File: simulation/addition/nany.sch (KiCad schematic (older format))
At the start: 6 parts, among them M2 MPMOS, M3 MPMOS, M4 MNMOS, M5 MNMOS

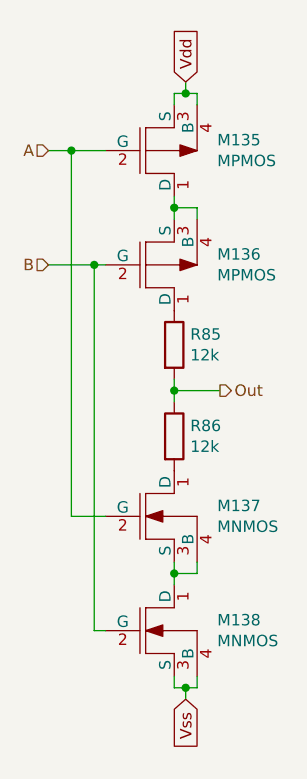
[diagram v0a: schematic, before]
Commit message: remove nconensus gate from sum gate, removed .sch-bak and cache files
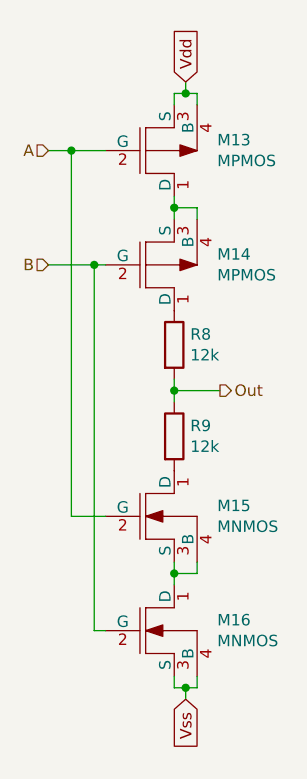
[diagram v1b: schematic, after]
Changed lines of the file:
@@
 $Descr A4 11693 8268
 encoding utf-8
-Sheet 7 28
+Sheet 7 26
 Title ""
 Date ""
@@
 AR Path="/5FDE2F92/5FDD79FE/5FEDF3F0/600EB164/5FFEAE4F" Ref="M606"  Part="1"
 AR Path="/5FDE2F92/5FDD8DDE/5FFEAE4F" Ref="M626"  Part="1"
-F 0 "M136" H 5688 3396 50  0000 L CNN
+AR Path="/5FDC5271/600A11DE/5FFEAE4F" Ref="M6"  Part="1"
+AR Path="/5FDC5271/600E751A/5FFEAE4F" Ref="M10"  Part="1"
+AR Path="/5FDC5271/600EB164/5FFEAE4F" Ref="M14"  Part="1"
+F 0 "M14" H 5688 3396 50  0000 L CNN
 F 1 "MPMOS" H 5688 3305 50  0000 L CNN
 F 2 "" H 5400 3350 50  0001 C CNN
@@
 AR Path="/5FDE2F92/5FDD79FE/5FEDF3F0/600EB164/5FFEAE59" Ref="M607"  Part="1"
 AR Path="/5FDE2F92/5FDD8DDE/5FFEAE59" Ref="M627"  Part="1"
-F 0 "M137" H 5688 4496 50  0000 L CNN
+AR Path="/5FDC5271/600A11DE/5FFEAE59" Ref="M7"  Part="1"
+AR Path="/5FDC5271/600E751A/5FFEAE59" Ref="M11"  Part="1"
+AR Path="/5FDC5271/600EB164/5FFEAE59" Ref="M15"  Part="1"
+F 0 "M15" H 5688 4496 50  0000 L CNN
 F 1 "MNMOS" H 5688 4405 50  0000 L CNN
 F 2 "" H 5375 4450 50  0001 C CNN
@@
 AR Path="/5FDE2F92/5FDD79FE/5FEDF3F0/600EB164/5FFEAE68" Ref="R380"  Part="1"
 AR Path="/5FDE2F92/5FDD8DDE/5FFEAE68" Ref="R394"  Part="1"
-F 0 "R86" H 5570 4146 50  0000 L CNN
+AR Path="/5FDC5271/600A11DE/5FFEAE68" Ref="R5"  Part="1"
+AR Path="/5FDC5271/600E751A/5FFEAE68" Ref="R7"  Part="1"
+AR Path="/5FDC5271/600EB164/5FFEAE68" Ref="R9"  Part="1"
+F 0 "R9" H 5570 4146 50  0000 L CNN
 F 1 "12k" H 5570 4055 50  0000 L CNN
 F 2 "" V 5430 4100 50  0001 C CNN
@@
 AR Path="/5FDE2F92/5FDD79FE/5FEDF3F0/600EB164/5FFEAE6E" Ref="R379"  Part="1"
 AR Path="/5FDE2F92/5FDD8DDE/5FFEAE6E" Ref="R393"  Part="1"
-F 0 "R85" H 5570 3746 50  0000 L CNN
+AR Path="/5FDC5271/600A11DE/5FFEAE6E" Ref="R4"  Part="1"
+AR Path="/5FDC5271/600E751A/5FFEAE6E" Ref="R6"  Part="1"
+AR Path="/5FDC5271/600EB164/5FFEAE6E" Ref="R8"  Part="1"
+F 0 "R8" H 5570 3746 50  0000 L CNN
 F 1 "12k" H 5570 3655 50  0000 L CNN
 F 2 "" V 5430 3700 50  0001 C CNN
@@
 AR Path="/5FDE2F92/5FDD79FE/5FEDF3F0/600EB164/5FFEAE7E" Ref="M608"  Part="1"
 AR Path="/5FDE2F92/5FDD8DDE/5FFEAE7E" Ref="M628"  Part="1"
-F 0 "M138" H 5688 4996 50  0000 L CNN
+AR Path="/5FDC5271/600A11DE/5FFEAE7E" Ref="M8"  Part="1"
+AR Path="/5FDC5271/600E751A/5FFEAE7E" Ref="M12"  Part="1"
+AR Path="/5FDC5271/600EB164/5FFEAE7E" Ref="M16"  Part="1"
+F 0 "M16" H 5688 4996 50  0000 L CNN
 F 1 "MNMOS" H 5688 4905 50  0000 L CNN
 F 2 "" H 5375 4950 50  0001 C CNN
@@
 AR Path="/5FDE2F92/5FDD79FE/5FEDF3F0/600EB164/5FFEAE96" Ref="M605"  Part="1"
 AR Path="/5FDE2F92/5FDD8DDE/5FFEAE96" Ref="M625"  Part="1"
-F 0 "M135" H 5688 2896 50  0000 L CNN
+AR Path="/5FDC5271/600A11DE/5FFEAE96" Ref="M5"  Part="1"
+AR Path="/5FDC5271/600E751A/5FFEAE96" Ref="M9"  Part="1"
+AR Path="/5FDC5271/600EB164/5FFEAE96" Ref="M13"  Part="1"
+F 0 "M13" H 5688 2896 50  0000 L CNN
 F 1 "MPMOS" H 5688 2805 50  0000 L CNN
 F 2 "" H 5400 2850 50  0001 C CNN

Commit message: lowered transistor count for sum gate
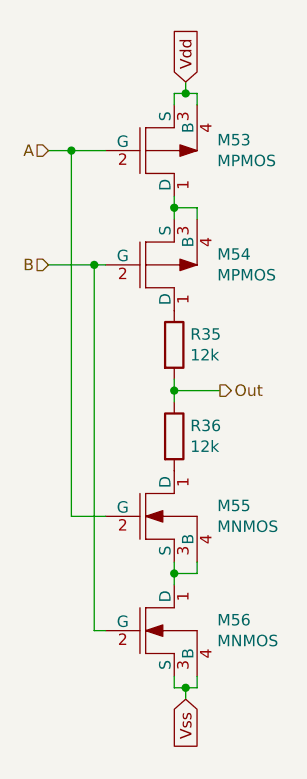
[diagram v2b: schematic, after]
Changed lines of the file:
@@
 $Descr A4 11693 8268
 encoding utf-8
-Sheet 7 26
+Sheet 7 24
 Title ""
 Date ""
@@
 AR Path="/5FDC5271/600E751A/5FFEAE4F" Ref="M10"  Part="1"
 AR Path="/5FDC5271/600EB164/5FFEAE4F" Ref="M14"  Part="1"
-F 0 "M14" H 5688 3396 50  0000 L CNN
+AR Path="/5FDCD92F/600A11DE/5FFEAE4F" Ref="M6"  Part="1"
+AR Path="/5FDCD92F/600E751A/5FFEAE4F" Ref="M10"  Part="1"
+AR Path="/5FDCD92F/600EB164/5FFEAE4F" Ref="M14"  Part="1"
+AR Path="/5FDCD92F/5FDCFF59/5FFEAE4F" Ref="M?"  Part="1"
+AR Path="/5FDD3C70/5FDA8800/5FEDF3F0/600A11DE/5FFEAE4F" Ref="M2"  Part="1"
+AR Path="/5FDD3C70/5FDA8800/5FEDF3F0/600E751A/5FFEAE4F" Ref="M6"  Part="1"
+AR Path="/5FDD3C70/5FDA8800/5FEDF3F0/600EB164/5FFEAE4F" Ref="M10"  Part="1"
+AR Path="/5FDD3C70/5FDD79FE/5FEDF3F0/600A11DE/5FFEAE4F" Ref="M28"  Part="1"
+AR Path="/5FDD3C70/5FDD79FE/5FEDF3F0/600E751A/5FFEAE4F" Ref="M32"  Part="1"
+AR Path="/5FDD3C70/5FDD79FE/5FEDF3F0/600EB164/5FFEAE4F" Ref="M36"  Part="1"
+AR Path="/5FDD3C70/5FDD8DDE/5FFEAE4F" Ref="M54"  Part="1"
+F 0 "M54" H 5688 3396 50  0000 L CNN
 F 1 "MPMOS" H 5688 3305 50  0000 L CNN
 F 2 "" H 5400 3350 50  0001 C CNN
@@
 AR Path="/5FDC5271/600E751A/5FFEAE59" Ref="M11"  Part="1"
 AR Path="/5FDC5271/600EB164/5FFEAE59" Ref="M15"  Part="1"
-F 0 "M15" H 5688 4496 50  0000 L CNN
+AR Path="/5FDCD92F/600A11DE/5FFEAE59" Ref="M7"  Part="1"
+AR Path="/5FDCD92F/600E751A/5FFEAE59" Ref="M11"  Part="1"
+AR Path="/5FDCD92F/600EB164/5FFEAE59" Ref="M15"  Part="1"
+AR Path="/5FDCD92F/5FDCFF59/5FFEAE59" Ref="M?"  Part="1"
+AR Path="/5FDD3C70/5FDA8800/5FEDF3F0/600A11DE/5FFEAE59" Ref="M3"  Part="1"
+AR Path="/5FDD3C70/5FDA8800/5FEDF3F0/600E751A/5FFEAE59" Ref="M7"  Part="1"
+AR Path="/5FDD3C70/5FDA8800/5FEDF3F0/600EB164/5FFEAE59" Ref="M11"  Part="1"
+AR Path="/5FDD3C70/5FDD79FE/5FEDF3F0/600A11DE/5FFEAE59" Ref="M29"  Part="1"
+AR Path="/5FDD3C70/5FDD79FE/5FEDF3F0/600E751A/5FFEAE59" Ref="M33"  Part="1"
+AR Path="/5FDD3C70/5FDD79FE/5FEDF3F0/600EB164/5FFEAE59" Ref="M37"  Part="1"
+AR Path="/5FDD3C70/5FDD8DDE/5FFEAE59" Ref="M55"  Part="1"
+F 0 "M55" H 5688 4496 50  0000 L CNN
 F 1 "MNMOS" H 5688 4405 50  0000 L CNN
 F 2 "" H 5375 4450 50  0001 C CNN
@@
 AR Path="/5FDC5271/600E751A/5FFEAE68" Ref="R7"  Part="1"
 AR Path="/5FDC5271/600EB164/5FFEAE68" Ref="R9"  Part="1"
-F 0 "R9" H 5570 4146 50  0000 L CNN
+AR Path="/5FDCD92F/600A11DE/5FFEAE68" Ref="R6"  Part="1"
+AR Path="/5FDCD92F/600E751A/5FFEAE68" Ref="R8"  Part="1"
+AR Path="/5FDCD92F/600EB164/5FFEAE68" Ref="R10"  Part="1"
+AR Path="/5FDCD92F/5FDCFF59/5FFEAE68" Ref="R?"  Part="1"
+AR Path="/5FDD3C70/5FDA8800/5FEDF3F0/600A11DE/5FFEAE68" Ref="R3"  Part="1"
+AR Path="/5FDD3C70/5FDA8800/5FEDF3F0/600E751A/5FFEAE68" Ref="R6"  Part="1"
+AR Path="/5FDD3C70/5FDA8800/5FEDF3F0/600EB164/5FFEAE68" Ref="R8"  Part="1"
+AR Path="/5FDD3C70/5FDD79FE/5FEDF3F0/600A11DE/5FFEAE68" Ref="R20"  Part="1"
+AR Path="/5FDD3C70/5FDD79FE/5FEDF3F0/600E751A/5FFEAE68" Ref="R22"  Part="1"
+AR Path="/5FDD3C70/5FDD79FE/5FEDF3F0/600EB164/5FFEAE68" Ref="R24"  Part="1"
+AR Path="/5FDD3C70/5FDD8DDE/5FFEAE68" Ref="R36"  Part="1"
+F 0 "R36" H 5570 4146 50  0000 L CNN
 F 1 "12k" H 5570 4055 50  0000 L CNN
 F 2 "" V 5430 4100 50  0001 C CNN
@@
 AR Path="/5FDC5271/600E751A/5FFEAE6E" Ref="R6"  Part="1"
 AR Path="/5FDC5271/600EB164/5FFEAE6E" Ref="R8"  Part="1"
-F 0 "R8" H 5570 3746 50  0000 L CNN
+AR Path="/5FDCD92F/600A11DE/5FFEAE6E" Ref="R4"  Part="1"
+AR Path="/5FDCD92F/600E751A/5FFEAE6E" Ref="R7"  Part="1"
+AR Path="/5FDCD92F/600EB164/5FFEAE6E" Ref="R9"  Part="1"
+AR Path="/5FDCD92F/5FDCFF59/5FFEAE6E" Ref="R?"  Part="1"
+AR Path="/5FDD3C70/5FDA8800/5FEDF3F0/600A11DE/5FFEAE6E" Ref="R1"  Part="1"
+AR Path="/5FDD3C70/5FDA8800/5FEDF3F0/600E751A/5FFEAE6E" Ref="R4"  Part="1"
+AR Path="/5FDD3C70/5FDA8800/5FEDF3F0/600EB164/5FFEAE6E" Ref="R7"  Part="1"
+AR Path="/5FDD3C70/5FDD79FE/5FEDF3F0/600A11DE/5FFEAE6E" Ref="R19"  Part="1"
+AR Path="/5FDD3C70/5FDD79FE/5FEDF3F0/600E751A/5FFEAE6E" Ref="R21"  Part="1"
+AR Path="/5FDD3C70/5FDD79FE/5FEDF3F0/600EB164/5FFEAE6E" Ref="R23"  Part="1"
+AR Path="/5FDD3C70/5FDD8DDE/5FFEAE6E" Ref="R35"  Part="1"
+F 0 "R35" H 5570 3746 50  0000 L CNN
 F 1 "12k" H 5570 3655 50  0000 L CNN
 F 2 "" V 5430 3700 50  0001 C CNN
@@
 AR Path="/5FDC5271/600E751A/5FFEAE7E" Ref="M12"  Part="1"
 AR Path="/5FDC5271/600EB164/5FFEAE7E" Ref="M16"  Part="1"
-F 0 "M16" H 5688 4996 50  0000 L CNN
+AR Path="/5FDCD92F/600A11DE/5FFEAE7E" Ref="M8"  Part="1"
+AR Path="/5FDCD92F/600E751A/5FFEAE7E" Ref="M12"  Part="1"
+AR Path="/5FDCD92F/600EB164/5FFEAE7E" Ref="M16"  Part="1"
+AR Path="/5FDCD92F/5FDCFF59/5FFEAE7E" Ref="M?"  Part="1"
+AR Path="/5FDD3C70/5FDA8800/5FEDF3F0/600A11DE/5FFEAE7E" Ref="M4"  Part="1"
+AR Path="/5FDD3C70/5FDA8800/5FEDF3F0/600E751A/5FFEAE7E" Ref="M8"  Part="1"
+AR Path="/5FDD3C70/5FDA8800/5FEDF3F0/600EB164/5FFEAE7E" Ref="M12"  Part="1"
+AR Path="/5FDD3C70/5FDD79FE/5FEDF3F0/600A11DE/5FFEAE7E" Ref="M30"  Part="1"
+AR Path="/5FDD3C70/5FDD79FE/5FEDF3F0/600E751A/5FFEAE7E" Ref="M34"  Part="1"
+AR Path="/5FDD3C70/5FDD79FE/5FEDF3F0/600EB164/5FFEAE7E" Ref="M38"  Part="1"
+AR Path="/5FDD3C70/5FDD8DDE/5FFEAE7E" Ref="M56"  Part="1"
+F 0 "M56" H 5688 4996 50  0000 L CNN
 F 1 "MNMOS" H 5688 4905 50  0000 L CNN
 F 2 "" H 5375 4950 50  0001 C CNN
@@
 AR Path="/5FDC5271/600E751A/5FFEAE96" Ref="M9"  Part="1"
 AR Path="/5FDC5271/600EB164/5FFEAE96" Ref="M13"  Part="1"
-F 0 "M13" H 5688 2896 50  0000 L CNN
+AR Path="/5FDCD92F/600A11DE/5FFEAE96" Ref="M5"  Part="1"
+AR Path="/5FDCD92F/600E751A/5FFEAE96" Ref="M9"  Part="1"
+AR Path="/5FDCD92F/600EB164/5FFEAE96" Ref="M13"  Part="1"
+AR Path="/5FDCD92F/5FDCFF59/5FFEAE96" Ref="M?"  Part="1"
+AR Path="/5FDD3C70/5FDA8800/5FEDF3F0/600A11DE/5FFEAE96" Ref="M1"  Part="1"
+AR Path="/5FDD3C70/5FDA8800/5FEDF3F0/600E751A/5FFEAE96" Ref="M5"  Part="1"
+AR Path="/5FDD3C70/5FDA8800/5FEDF3F0/600EB164/5FFEAE96" Ref="M9"  Part="1"
+AR Path="/5FDD3C70/5FDD79FE/5FEDF3F0/600A11DE/5FFEAE96" Ref="M27"  Part="1"
+AR Path="/5FDD3C70/5FDD79FE/5FEDF3F0/600E751A/5FFEAE96" Ref="M31"  Part="1"
+AR Path="/5FDD3C70/5FDD79FE/5FEDF3F0/600EB164/5FFEAE96" Ref="M35"  Part="1"
+AR Path="/5FDD3C70/5FDD8DDE/5FFEAE96" Ref="M53"  Part="1"
+F 0 "M53" H 5688 2896 50  0000 L CNN
 F 1 "MPMOS" H 5688 2805 50  0000 L CNN
 F 2 "" H 5400 2850 50  0001 C CNN
